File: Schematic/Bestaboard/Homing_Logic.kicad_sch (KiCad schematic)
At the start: 4 parts, among them U4 CD40107BE, U5 CD4081BE

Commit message: Moved local copy schematic into repo.
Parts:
- removed R3, R4: 10K, Resistor_SMD:R_0805_2012Metric_Pad1.20x1.40mm_HandSolder, symbol Device:R_Small_US
- removed U4: CD40107BE, Package_DIP:DIP-8_W7.62mm_LongPads, symbol Bestaboard_Components:CD40107BE
- added C6, C7, C8: 0.1uF, Capacitor_SMD:C_0603_1608Metric_Pad1.08x0.95mm_HandSolder, symbol Device:C_US
- added U10: SN74HC32N, Package_DIP:DIP-14_W7.62mm_LongPads, symbol 74xx:74HC04
- added U4: SN74HC00N, Package_DIP:DIP-14_W7.62mm_LongPads, symbol 74xx:74HC00
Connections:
- net +5V: now also C6.1, C7.1, C8.1, U10.1, U10.11, U10.13, U10.14 (VCC), U10.3, U4.10, U4.14 (VCC), U4.4, U4.5, U4.9
- net GND: now also C6.2, C7.2, C8.2, U10.7 (GND), U4.7 (GND)
- net HOME: now also U4.1, U4.13
- net LEFT_HOMED: now also U10.6, U4.2
- net RIGHT_HOMED: now also U10.8, U4.12
- net at U5.8: now also U4.11
- net at U5.1: now also U4.3
- new net LEFT_HOMED_n: U10.5
- new net RIGHT_HOMED_n: U10.9
- no-connect marks 0 -> 6
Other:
- note added: "Decoupling for ICs, place next to devices"
- moved on the sheet: U5E

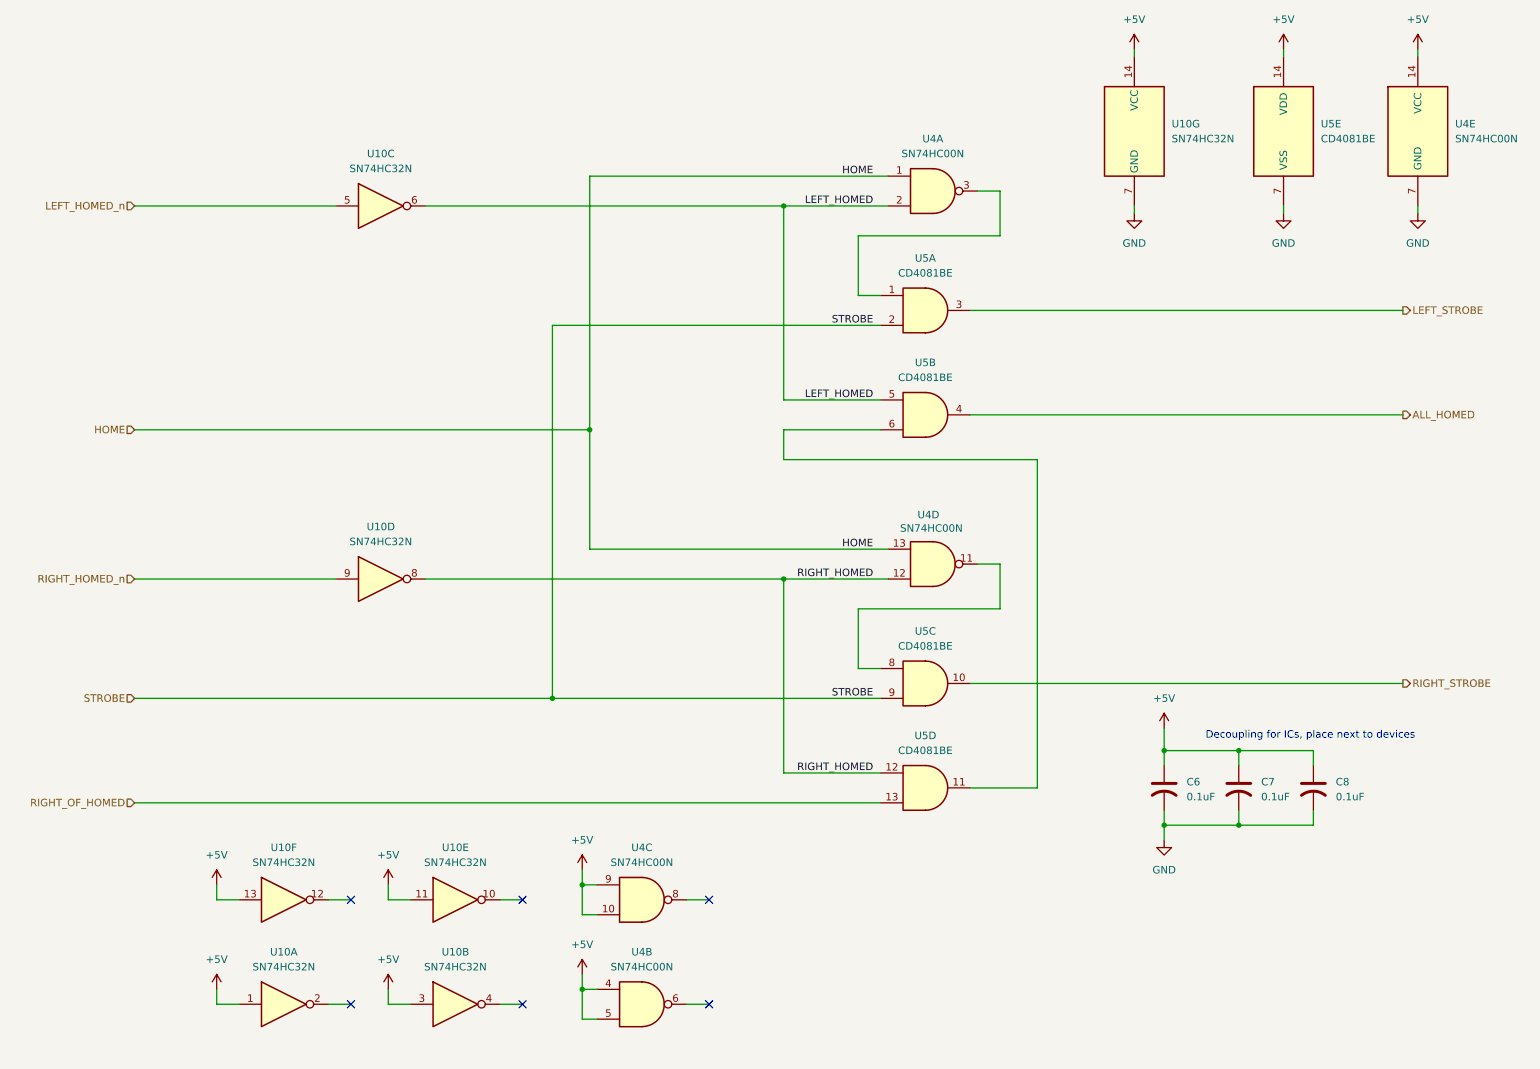
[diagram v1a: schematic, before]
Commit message: Prints, Schematic, PCB, Code Update
Prints - Created print plates for flips, drum and frame, updated frame to have mounting holes on the bottom.
PCB/Schematic - Changed to 14 pin NAND chip, updated parameters.
Code - Changed code to alternate between homing and character rotation.
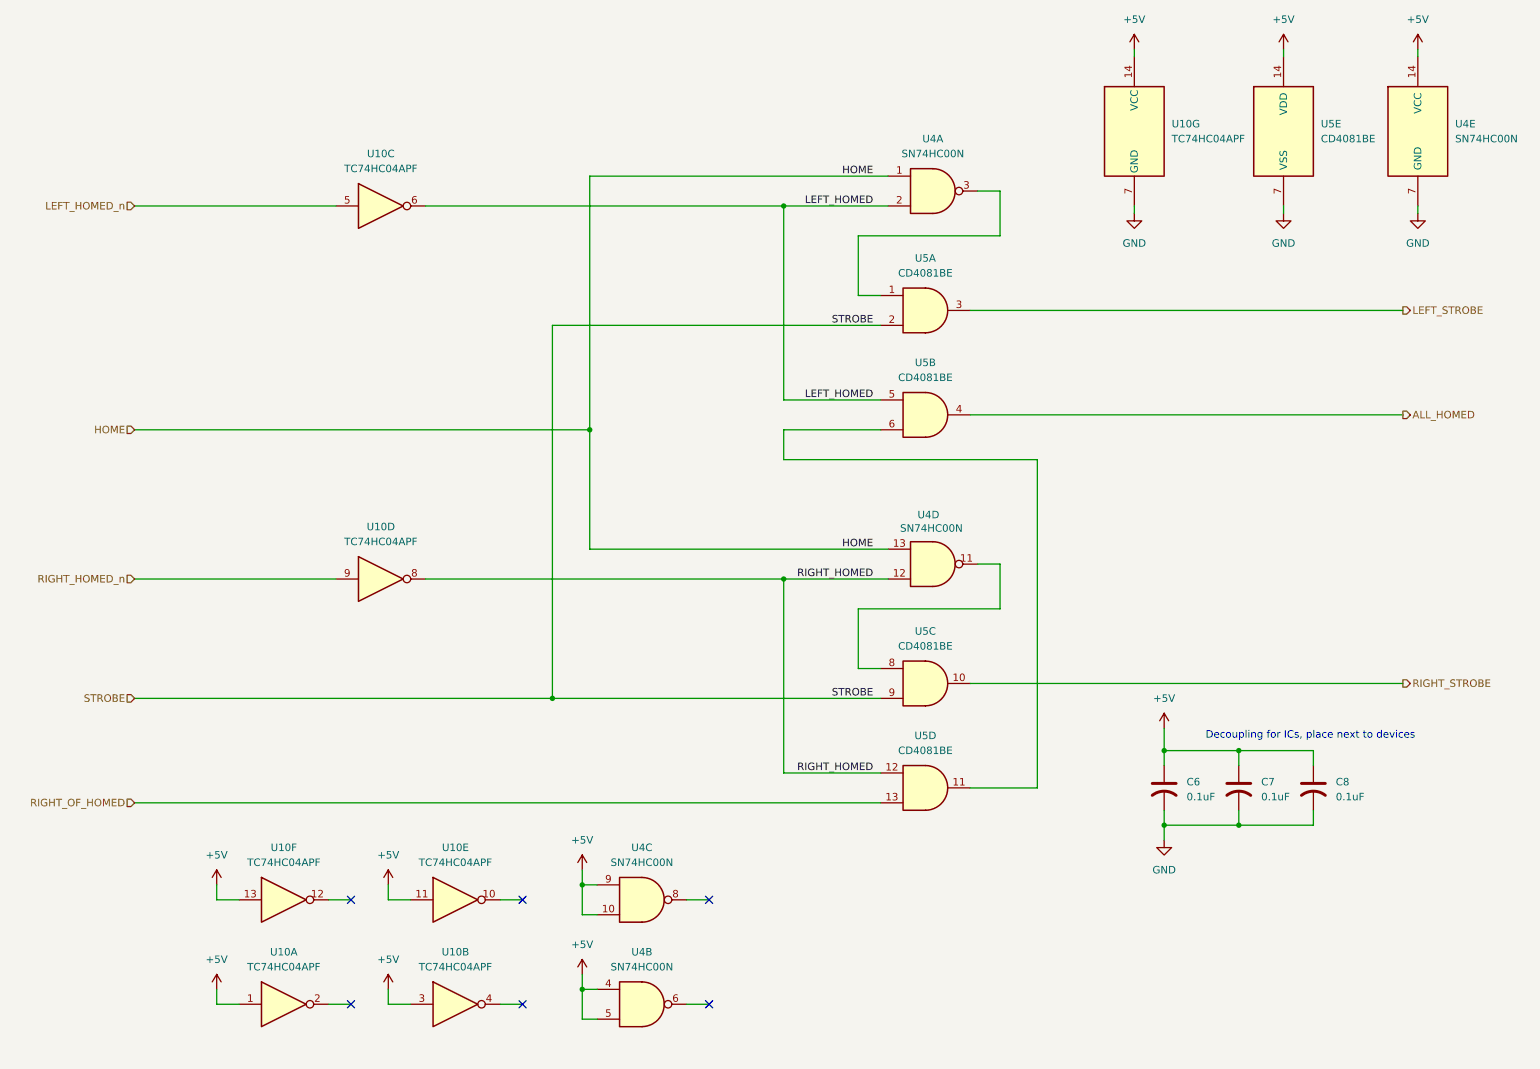
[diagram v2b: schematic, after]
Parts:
- U10: value SN74HC32N -> TC74HC04APF
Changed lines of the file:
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@@
 			)
 		)
-		(property "Datasheet" ""
+		(property "Datasheet" "https://www.ti.com/general/docs/suppproductinfo.tsp?distId=10&gotoUrl=https%3A%2F%2Fwww.ti.com%2Flit%2Fgpn%2Fcd4073b"
 			(at 233.68 38.1 0)
 			(effects
@@
 			)
 		)
-		(property "Datasheet" "http://www.ti.com/lit/gpn/sn74hc00"
+		(property "Datasheet" "https://www.ti.com/lit/ds/symlink/sn74hc00.pdf?HQS=dis-dk-null-digikeymode-dsf-pf-null-wwe&ts=1776325175776&ref_url=https%253A%252F%252Fwww.ti.com%252Fgeneral%252Fdocs%252Fsuppproductinfo.tsp%253FdistId%253D10%2526gotoUrl%253Dhttps%253A%252F%252Fwww.ti.com%252Flit%252Fgpn%252Fsn74hc00"
 			(at 173.99 48.26 0)
 			(effects
@@
 			)
 		)
-		(property "Datasheet" ""
+		(property "Datasheet" "https://yageogroup.com/content/datasheet/asset/file/KEM_C1002_X7R_SMD"
 			(at 213.36 149.86 0)
 			(effects
@@
 			)
 		)
-		(property "Datasheet" ""
+		(property "Datasheet" "https://www.ti.com/general/docs/suppproductinfo.tsp?distId=10&gotoUrl=https%3A%2F%2Fwww.ti.com%2Flit%2Fgpn%2Fcd4073b"
 			(at 172.72 68.58 0)
 			(effects
@@
 			)
 		)
-		(property "Datasheet" ""
+		(property "Datasheet" "https://www.ti.com/general/docs/suppproductinfo.tsp?distId=10&gotoUrl=https%3A%2F%2Fwww.ti.com%2Flit%2Fgpn%2Fcd4073b"
 			(at 172.72 86.36 0)
 			(effects
@@
 			)
 		)
-		(property "Value" "SN74HC32N"
+		(property "Value" "TC74HC04APF"
 			(at 92.71 162.56 0)
 			(effects
@@
 			)
 		)
-		(property "Datasheet" ""
+		(property "Datasheet" "https://mm.digikey.com/Volume0/opasdata/d220001/medias/docus/889/TC74HC04.pdf"
 			(at 92.71 168.91 0)
 			(effects
@@
 			)
 		)
-		(property "Value" "SN74HC32N"
+		(property "Value" "TC74HC04APF"
 			(at 63.5 162.56 0)
 			(effects
@@
 			)
 		)
-		(property "Datasheet" ""
+		(property "Datasheet" "https://mm.digikey.com/Volume0/opasdata/d220001/medias/docus/889/TC74HC04.pdf"
 			(at 63.5 168.91 0)
 			(effects
@@
 			)
 		)
-		(property "Datasheet" ""
+		(property "Datasheet" "https://www.ti.com/general/docs/suppproductinfo.tsp?distId=10&gotoUrl=https%3A%2F%2Fwww.ti.com%2Flit%2Fgpn%2Fcd4073b"
 			(at 172.72 149.86 0)
 			(effects
@@
 			)
 		)
-		(property "Datasheet" ""
+		(property "Datasheet" "https://yageogroup.com/content/datasheet/asset/file/KEM_C1002_X7R_SMD"
 			(at 226.06 149.86 0)
 			(effects
@@
 			)
 		)
-		(property "Value" "SN74HC32N"
+		(property "Value" "TC74HC04APF"
 			(at 80.01 107.95 0)
 			(effects
@@
 			)
 		)
-		(property "Datasheet" ""
+		(property "Datasheet" "https://mm.digikey.com/Volume0/opasdata/d220001/medias/docus/889/TC74HC04.pdf"
 			(at 80.01 114.3 0)
 			(effects
@@
 			)
 		)
-		(property "Datasheet" "http://www.ti.com/lit/gpn/sn74hc00"
+		(property "Datasheet" "https://www.ti.com/lit/ds/symlink/sn74hc00.pdf?HQS=dis-dk-null-digikeymode-dsf-pf-null-wwe&ts=1776325175776&ref_url=https%253A%252F%252Fwww.ti.com%252Fgeneral%252Fdocs%252Fsuppproductinfo.tsp%253FdistId%253D10%2526gotoUrl%253Dhttps%253A%252F%252Fwww.ti.com%252Flit%252Fgpn%252Fsn74hc00"
 			(at 256.54 38.1 0)
 			(effects
@@
 			)
 		)
-		(property "Value" "SN74HC32N"
+		(property "Value" "TC74HC04APF"
 			(at 63.5 180.34 0)
 			(effects
@@
 			)
 		)
-		(property "Datasheet" ""
+		(property "Datasheet" "https://mm.digikey.com/Volume0/opasdata/d220001/medias/docus/889/TC74HC04.pdf"
 			(at 63.5 186.69 0)
 			(effects
@@
 			)
 		)
-		(property "Datasheet" "http://www.ti.com/lit/gpn/sn74hc00"
+		(property "Datasheet" "https://www.ti.com/lit/ds/symlink/sn74hc00.pdf?HQS=dis-dk-null-digikeymode-dsf-pf-null-wwe&ts=1776325175776&ref_url=https%253A%252F%252Fwww.ti.com%252Fgeneral%252Fdocs%252Fsuppproductinfo.tsp%253FdistId%253D10%2526gotoUrl%253Dhttps%253A%252F%252Fwww.ti.com%252Flit%252Fgpn%252Fsn74hc00"
 			(at 173.99 111.76 0)
 			(effects
@@
 			)
 		)
-		(property "Datasheet" ""
+		(property "Datasheet" "https://yageogroup.com/content/datasheet/asset/file/KEM_C1002_X7R_SMD"
 			(at 238.76 149.86 0)
 			(effects
@@
 			)
 		)
-		(property "Value" "SN74HC32N"
+		(property "Value" "TC74HC04APF"
 			(at 80.01 44.45 0)
 			(effects
@@
 			)
 		)
-		(property "Datasheet" ""
+		(property "Datasheet" "https://mm.digikey.com/Volume0/opasdata/d220001/medias/docus/889/TC74HC04.pdf"
 			(at 80.01 50.8 0)
 			(effects
@@
 			)
 		)
-		(property "Value" "SN74HC32N"
+		(property "Value" "TC74HC04APF"
 			(at 214.63 39.3699 0)
 			(effects
@@
 			)
 		)
-		(property "Datasheet" ""
+		(property "Datasheet" "https://mm.digikey.com/Volume0/opasdata/d220001/medias/docus/889/TC74HC04.pdf"
 			(at 208.28 38.1 0)
 			(effects
@@
 			)
 		)
-		(property "Value" "SN74HC32N"
+		(property "Value" "TC74HC04APF"
 			(at 92.71 180.34 0)
 			(effects
@@
 			)
 		)
-		(property "Datasheet" ""
+		(property "Datasheet" "https://mm.digikey.com/Volume0/opasdata/d220001/medias/docus/889/TC74HC04.pdf"
 			(at 92.71 186.69 0)
 			(effects
@@
 			)
 		)
-		(property "Datasheet" "http://www.ti.com/lit/gpn/sn74hc00"
+		(property "Datasheet" "https://www.ti.com/lit/ds/symlink/sn74hc00.pdf?HQS=dis-dk-null-digikeymode-dsf-pf-null-wwe&ts=1776325175776&ref_url=https%253A%252F%252Fwww.ti.com%252Fgeneral%252Fdocs%252Fsuppproductinfo.tsp%253FdistId%253D10%2526gotoUrl%253Dhttps%253A%252F%252Fwww.ti.com%252Flit%252Fgpn%252Fsn74hc00"
 			(at 124.46 186.69 0)
 			(effects
@@
 			)
 		)
-		(property "Datasheet" ""
+		(property "Datasheet" "https://www.ti.com/general/docs/suppproductinfo.tsp?distId=10&gotoUrl=https%3A%2F%2Fwww.ti.com%2Flit%2Fgpn%2Fcd4073b"
 			(at 172.72 132.08 0)
 			(effects
@@
 			)
 		)
-		(property "Datasheet" "http://www.ti.com/lit/gpn/sn74hc00"
+		(property "Datasheet" "https://www.ti.com/lit/ds/symlink/sn74hc00.pdf?HQS=dis-dk-null-digikeymode-dsf-pf-null-wwe&ts=1776325175776&ref_url=https%253A%252F%252Fwww.ti.com%252Fgeneral%252Fdocs%252Fsuppproductinfo.tsp%253FdistId%253D10%2526gotoUrl%253Dhttps%253A%252F%252Fwww.ti.com%252Flit%252Fgpn%252Fsn74hc00"
 			(at 124.46 168.91 0)
 			(effects

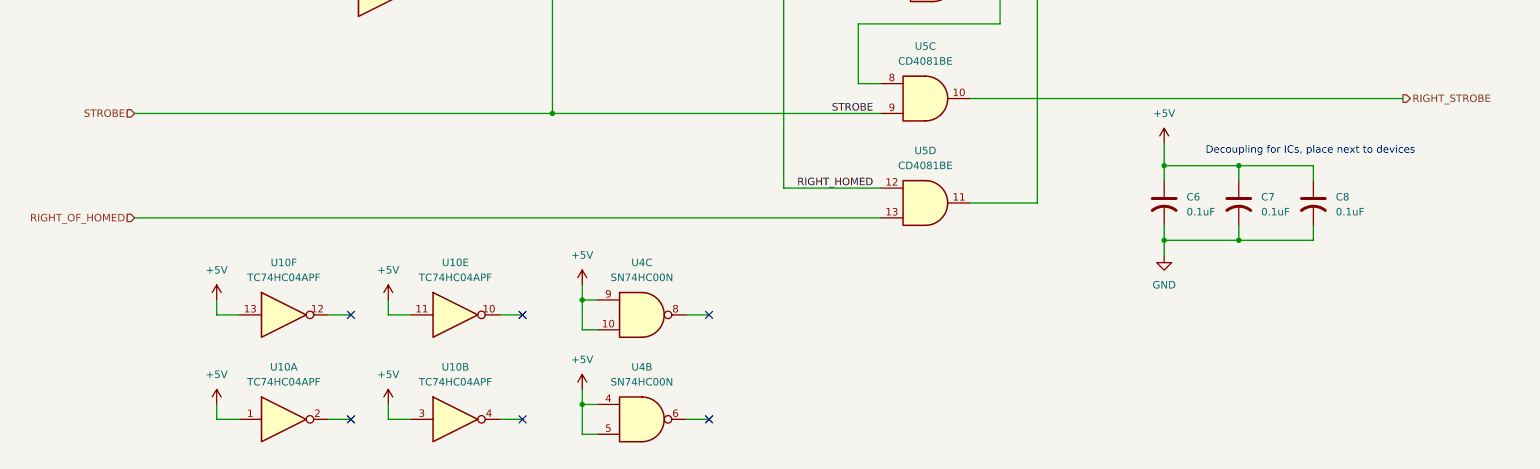
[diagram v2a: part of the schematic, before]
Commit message: Output BOM and updated parts list
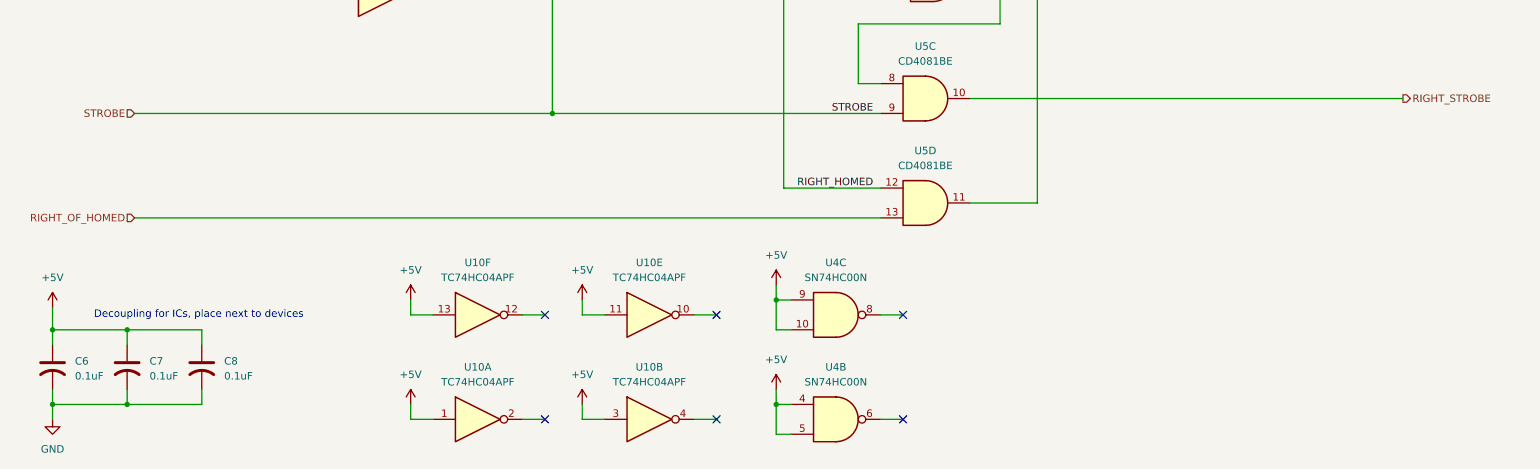
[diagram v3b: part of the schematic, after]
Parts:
- C6, C7, C8: Purchase Link (none) -> https://www.digikey.com/en/products/detail/kemet/C0603C104K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
- U10: Purchase Link (none) -> https://www.digikey.com/en/products/detail/toshiba-semicond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
- U4, U5: Purchase Link (none) -> https://www.digikey.com/en/products/detail/texas-instrument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
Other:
- moved on the sheet: C6, C7, C8, U10A, U10B, U10E, U10F, U4B, U4C

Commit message: Schematic PDF & Schematic
Updated title block to include date and name. Created PDF of scheamtic.
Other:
- company: (none) -> Isaac Rasmusson
- title: (none) -> Bestaboard
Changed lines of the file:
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@@
 	(generator_version "9.0")
 	(paper "A4")
+	(title_block
+		(title "Bestaboard")
+		(date "2026-05-21")
+		(rev "A")
+		(company "Isaac Rasmusson")
+	)
 	(text "Decoupling for ICs, place next to devices"
 		(exclude_from_sim no)
